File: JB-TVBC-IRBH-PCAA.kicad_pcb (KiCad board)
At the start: 2 copper layers, 65 x 56 mm, 78 parts, among them J1 CONN_2x20_FEM_100PITCH_635INS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, J2 SJ-435107, J3 SJ-435107, J4 SJ-435107, Q1 DMG2305UX-7, Q2 DMG2305UX-7, Q3 DMG2305UX-7, Q4 DMG2305UX-7, Q5 DMG2305UX-7, Q6 DMG2305UX-7, U1 CAT24C32, U2 LTC1693-5, U3 LTC1693-5, U4 LTC1693-5, U5 LTC1693-5, U6 LTC1693-5, U7 LTC1693-5

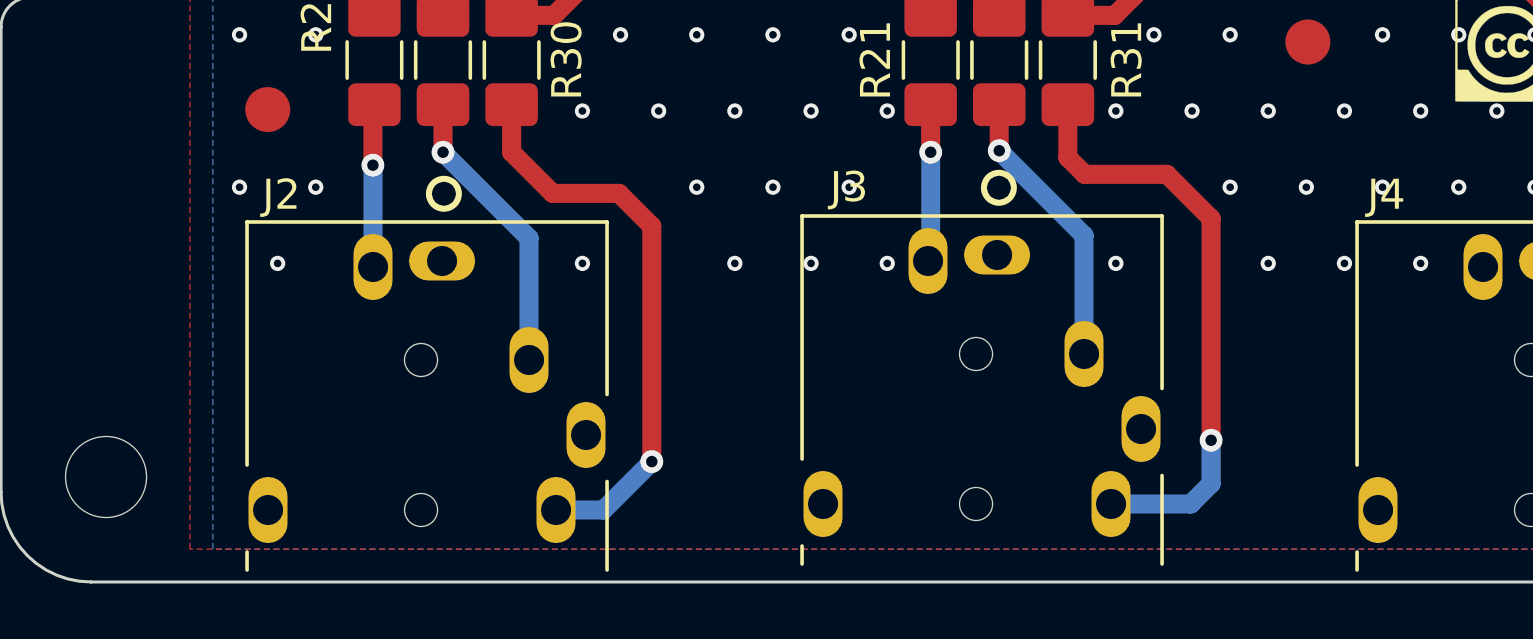
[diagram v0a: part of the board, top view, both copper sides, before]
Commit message: adding jack legend on silkscreen
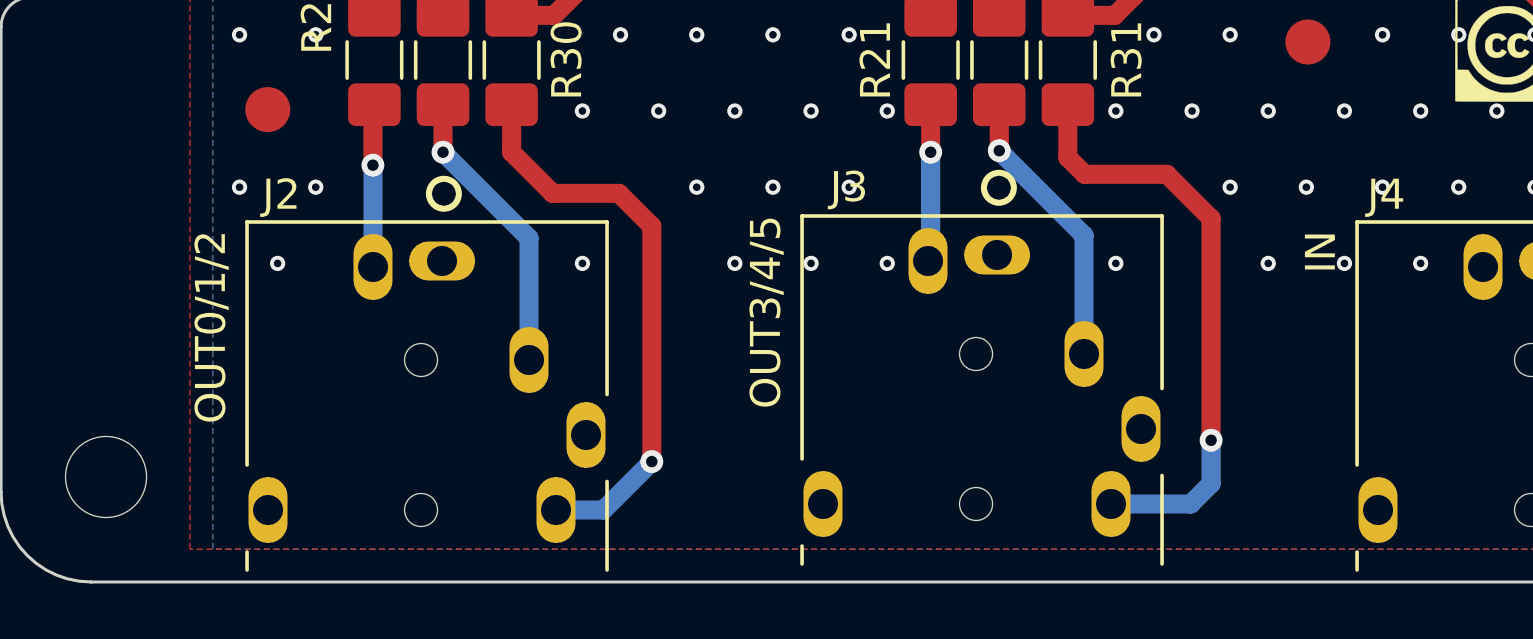
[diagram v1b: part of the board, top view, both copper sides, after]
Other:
- board text added: "IN"
- board text added: "OUT0/1/2"
- board text added: "OUT3/4/5"
